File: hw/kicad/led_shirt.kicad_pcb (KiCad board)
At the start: 2 copper layers, 26 parts, among them J1 10103593-0001LF, J2 2_PIN_HDR, J3 2_PIN_HDR, J4 5_PIN_HDR, Q1 PN_MOSFET_DUAL, SW1 SW_PUSH, U1 AP3012, U2 PIC12F1822, U3 MCP73831

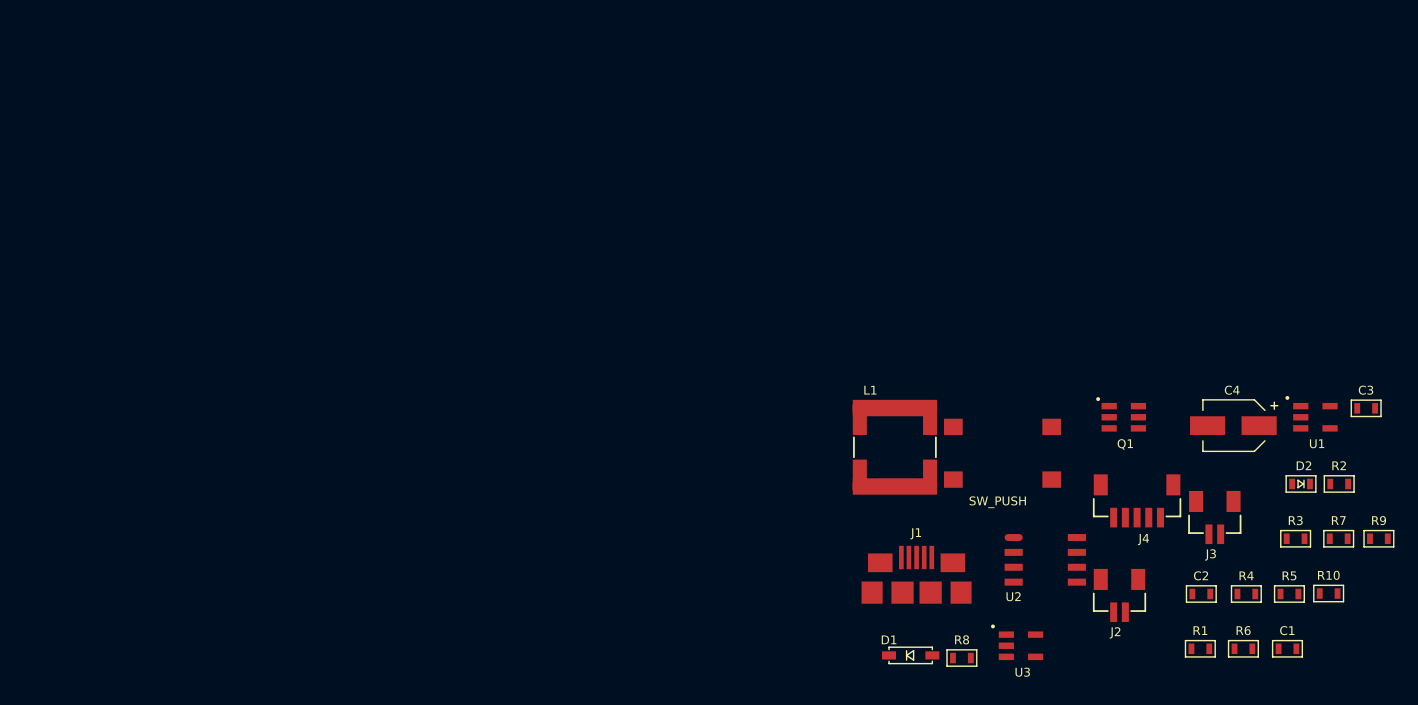
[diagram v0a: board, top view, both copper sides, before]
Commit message: parts positioned, silks. next is traces.
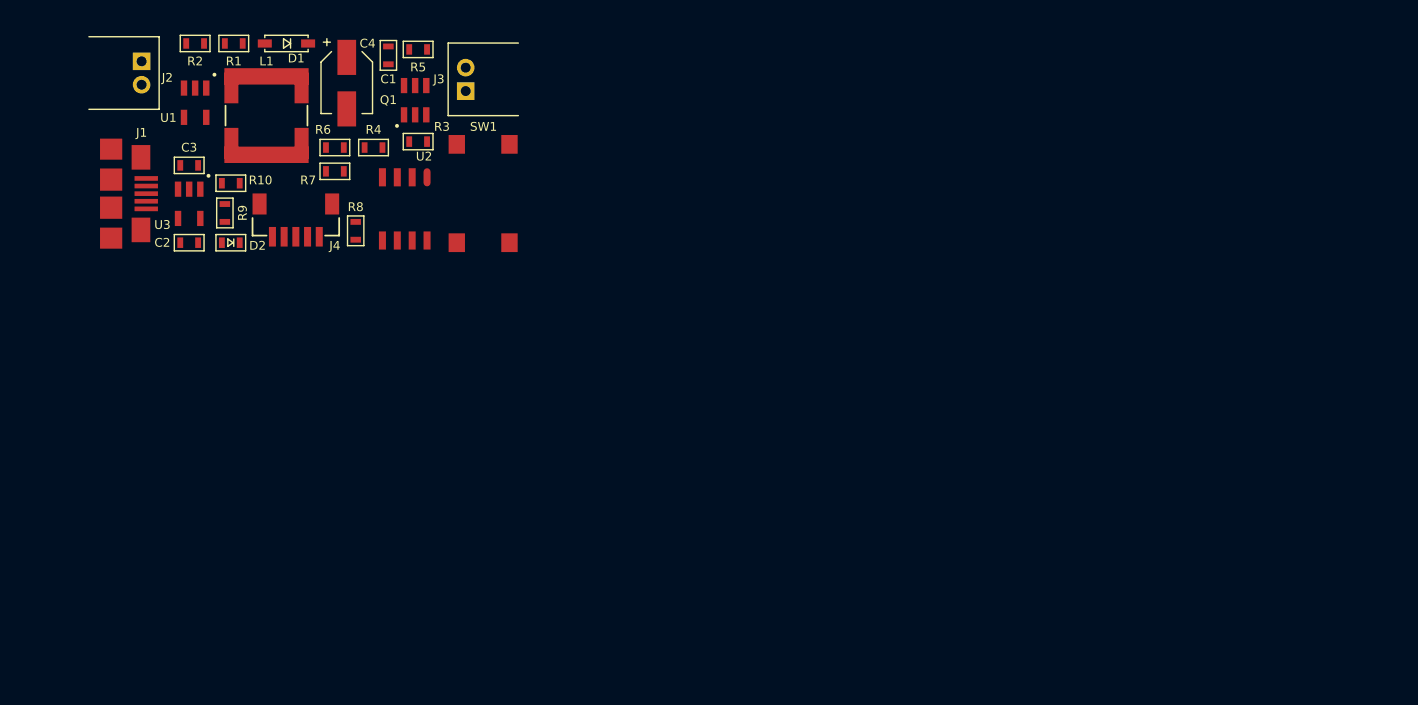
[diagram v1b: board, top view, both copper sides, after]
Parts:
- J2, J3: footprint kicadlib:SMD_JST_2_PIN_VERT -> kicadlib:TH_JST_2PIN_RIGHTANGLE
- moved R2 106.1 mm to (125.0, 79.0), turned to 180 degrees
- moved R9 103.4 mm to (128.3, 92.7), turned to 90 degrees
- moved C3 102.7 mm to (126.0, 89.4)
- moved R10 101.5 mm to (128.0, 90.9), turned to 180 degrees
- moved R1 98.7 mm to (128.3, 79.0), turned to 180 degrees
- moved U1 98.5 mm to (125.7, 82.8), turned to 270 degrees
- moved J2 95.4 mm to (121.2, 80.5), turned to 270 degrees
- moved D2 93.7 mm to (129.5, 96.0)
- moved C2 93.0 mm to (124.5, 96.0), turned to 180 degrees
- moved R7 92.7 mm to (136.9, 89.9), turned to 180 degrees
- moved C1 92.2 mm to (142.2, 80.8), turned to 270 degrees
- moved R6 90.0 mm to (136.9, 87.9), turned to 180 degrees
- moved R5 89.1 mm to (144.0, 79.5), turned to 180 degrees
- moved R4 85.1 mm to (140.2, 87.9), turned to 180 degrees
- moved R3 83.7 mm to (144.0, 87.4), turned to 180 degrees
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
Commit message: layout done
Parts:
- moved R5 1.48 mm to (144.8, 80.8), turned to 270 degrees
- moved U1 0.51 mm to (125.2, 82.8)
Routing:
- net GND: track 0.00 -> 76.3 mm, vias 0 -> 11
- net /vbat: track 0.00 -> 67.3 mm, vias 0 -> 1
- net /lps: track 0.00 -> 38.1 mm, vias 0 -> 3
- net /~lps_enable: track 0.00 -> 25.8 mm
- net /+12v: track 0.00 -> 22.5 mm
- net /icspdat: track 0.00 -> 15.9 mm, vias 0 -> 2
- net /led_cntrl: track 0.00 -> 14.1 mm, vias 0 -> 2
- net Net-(D1-Pad2): track 0.00 -> 13.8 mm
- net /icspclk: track 0.00 -> 12.7 mm, vias 0 -> 2
- net /mclr: track 0.00 -> 11.9 mm
- net /vbus: track 0.00 -> 10.8 mm
- net /batt_sns: track 0.00 -> 6.62 mm
- net Net-(R1-Pad2): track 0.00 -> 6.51 mm
- net Net-(D2-Pad2): track 0.00 -> 5.08 mm
- net /led-: track 0.00 -> 4.81 mm
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- added copper zone on B.Cu, net GND
- added copper zone on F.Cu, net GND

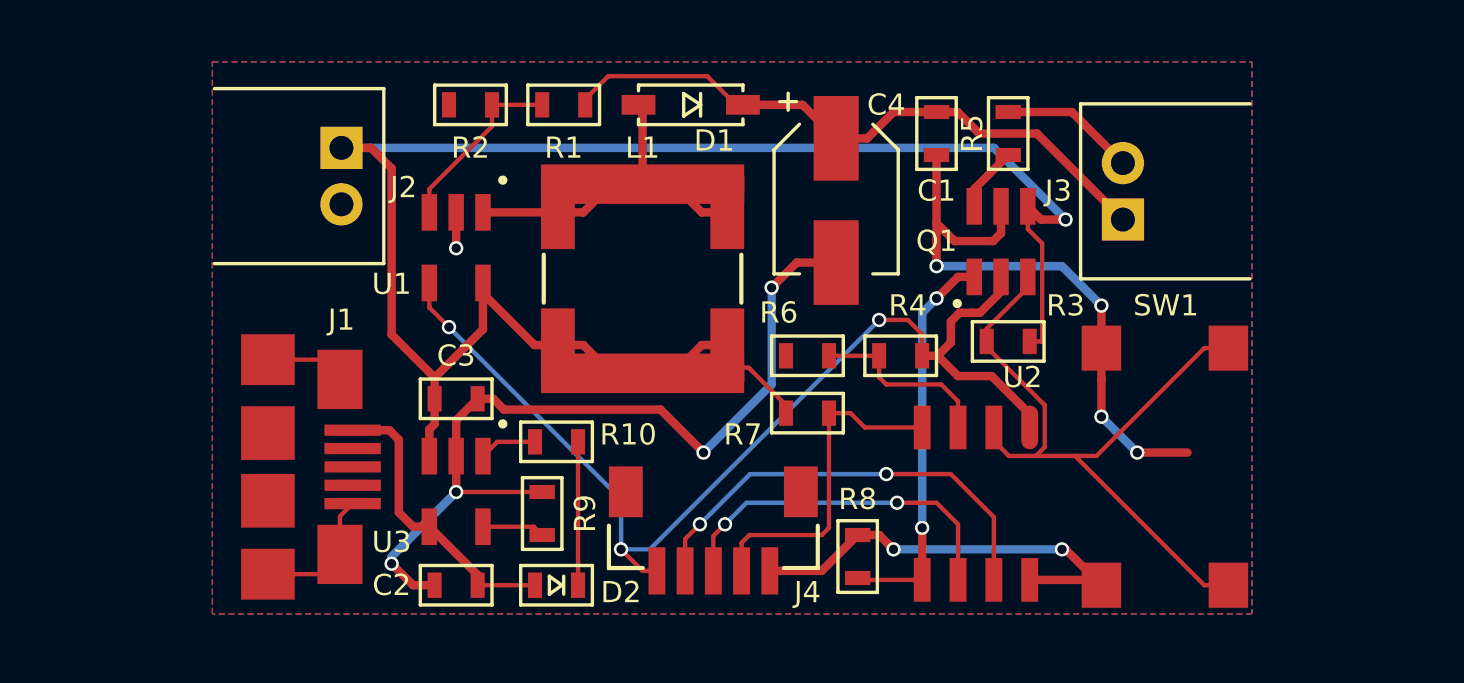
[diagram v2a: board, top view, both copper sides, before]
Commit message: add screw mounts, which adds $1.60 to osh price. also need to reposition usb connector if I use screw mounts.
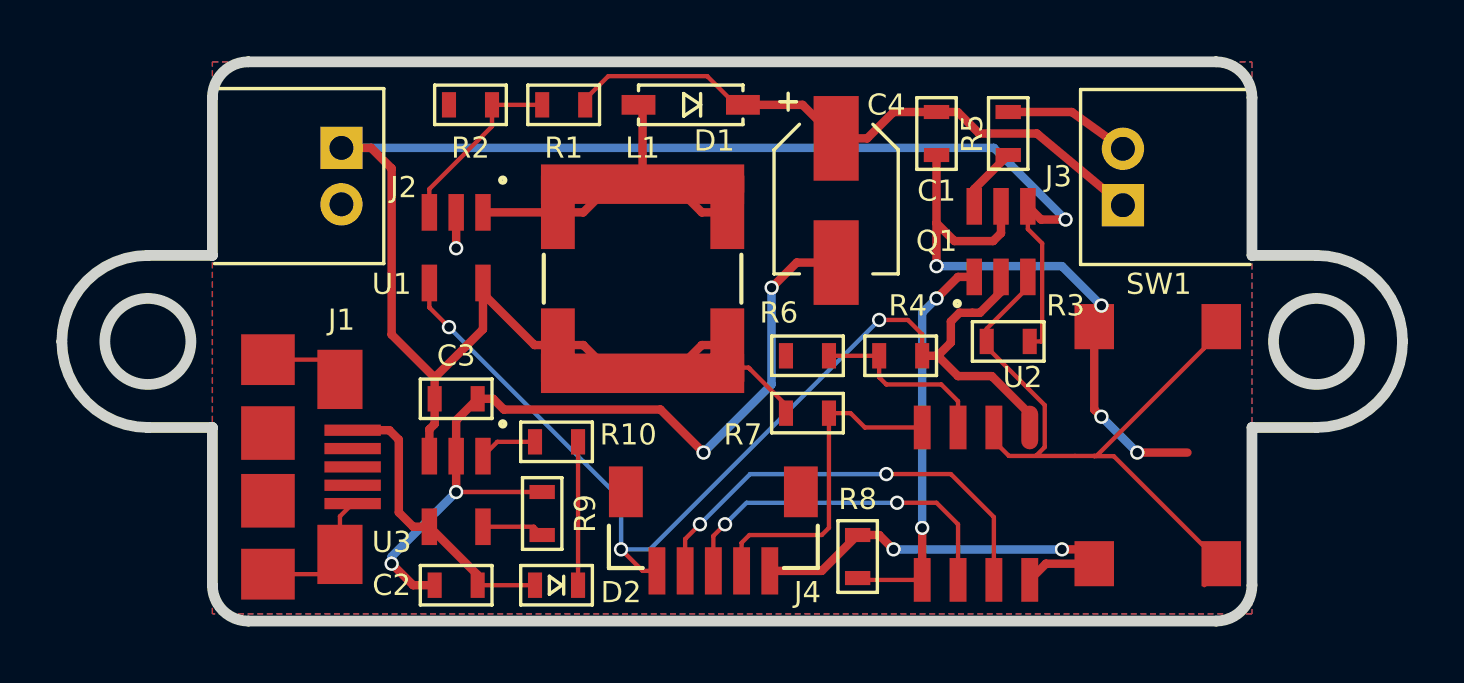
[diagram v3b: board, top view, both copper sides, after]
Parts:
- moved SW1 0.80 mm to (147.8, 95.2)
- moved J3 0.51 mm to (148.8, 82.5)
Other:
- board outline added: 47.5 x 19.8 mm
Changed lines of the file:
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@@
-(kicad_pcb (version 4) (host pcbnew 4.0.0-rc1-stable)
+(kicad_pcb (version 4) (host pcbnew 4.0.0-rc2-stable)
   (general
     (links 67)
     (no_connects 0)
-    (area 115.34578 76.46528 153.703721 98.16672)
+    (area 111.061499 77.279499 158.940501 97.472501)
     (thickness 1.6002)
-    (drawings 0)
-    (tracks 226)
+    (drawings 20)
+    (tracks 231)
     (zones 0)
     (modules 26)
@@
   )
   (module kicadlib:TH_JST_2PIN_RIGHTANGLE (layer Front)
-    (at 148.844 83.058 90)
+    (at 148.844 82.55 90)
     (fp_text reference J3 (at 1.016 -2.286 180) (layer F.SilkS)
       (effects (font (size 0.75 0.75) (thickness 0.12)))
@@
   )
   (module kicadlib:spst_pushbutton_smd placed (layer Front)
-    (at 148.082 96.012 90)
+    (at 147.828 95.25 90)
     (fp_text reference SW1 (at 9.906 2.286 180) (layer F.SilkS)
       (effects (font (size 0.75 0.75) (thickness 0.12)))
@@
     )
   )
-  (segment (start 145.796 80.01) (end 148.844 83.058) (width 0.29972) (layer Front) (net 1))
+  (gr_line (start 116.586 90.424) (end 116.586 96.012) (angle 90) (layer Edge.Cuts) (width 0.381))
+  (gr_line (start 116.586 78.74) (end 116.586 84.328) (angle 90) (layer Edge.Cuts) (width 0.381))
+  (gr_line (start 153.416 90.424) (end 153.416 96.012) (angle 90) (layer Edge.Cuts) (width 0.381))
+  (gr_line (start 153.416 78.74) (end 153.416 84.328) (angle 90) (layer Edge.Cuts) (width 0.381))
+  (gr_circle (center 114.3 87.376) (end 114.3 85.852) (layer Edge.Cuts) (width 0.381))
+  (gr_arc (start 114.3 87.376) (end 114.3 90.424) (angle 90) (layer Edge.Cuts) (width 0.381))
+  (gr_arc (start 114.3 87.376) (end 111.252 87.376) (angle 90) (layer Edge.Cuts) (width 0.381))
+  (gr_line (start 114.3 90.424) (end 116.586 90.424) (angle 90) (layer Edge.Cuts) (width 0.381))
+  (gr_line (start 114.3 84.328) (end 116.586 84.328) (angle 90) (layer Edge.Cuts) (width 0.381))
+  (gr_line (start 117.856 97.282) (end 152.146 97.282) (angle 90) (layer Edge.Cuts) (width 0.381))
+  (gr_line (start 155.702 90.424) (end 153.416 90.424) (angle 90) (layer Edge.Cuts) (width 0.381))
+  (gr_line (start 155.702 84.328) (end 153.416 84.328) (angle 90) (layer Edge.Cuts) (width 0.381))
+  (gr_arc (start 155.702 87.376) (end 158.75 87.376) (angle 90) (layer Edge.Cuts) (width 0.381))
+  (gr_arc (start 155.702 87.376) (end 155.702 84.328) (angle 90) (layer Edge.Cuts) (width 0.381))
+  (gr_circle (center 155.702 87.376) (end 155.702 88.9) (layer Edge.Cuts) (width 0.381))
+  (gr_line (start 152.146 77.47) (end 117.856 77.47) (angle 90) (layer Edge.Cuts) (width 0.381))
+  (gr_arc (start 117.856 96.012) (end 117.856 97.282) (angle 90) (layer Edge.Cuts) (width 0.381))
+  (gr_arc (start 152.146 96.012) (end 153.416 96.012) (angle 90) (layer Edge.Cuts) (width 0.381))
+  (gr_arc (start 152.146 78.74) (end 152.146 77.47) (angle 90) (layer Edge.Cuts) (width 0.381))
+  (gr_arc (start 117.856 78.74) (end 116.586 78.74) (angle 90) (layer Edge.Cuts) (width 0.381))
+  (segment (start 145.796 80.01) (end 148.844 82.55) (width 0.29972) (layer Front) (net 1) (status 20))
   (segment (start 143.75172 80.01) (end 145.796 80.01) (width 0.29972) (layer Front) (net 1))
   (segment (start 142.24 79.248) (end 142.98972 79.248) (width 0.29972) (layer Front) (net 1))
@@
   (segment (start 134.116 77.978) (end 135.132 78.994) (width 0.15494) (layer Front) (net 1))
   (segment (start 135.132 78.994) (end 135.382 78.994) (width 0.15494) (layer Front) (net 1))
+  (segment (start 148.082 90.043) (end 147.828 89.789) (width 0.29972) (layer Front) (net 2))
+  (via (at 148.082 90.043) (size 0.508) (drill 0.3302) (layers Front Back) (net 2))
+  (via (at 149.352 91.313) (size 0.508) (drill 0.3302) (layers Front Back) (net 2))
+  (segment (start 148.082 90.043) (end 149.352 91.313) (width 0.29972) (layer Back) (net 2))
+  (segment (start 151.13 91.313) (end 149.352 91.313) (width 0.29972) (layer Front) (net 2))
+  (segment (start 147.828 89.789) (end 147.828 86.85) (width 0.29972) (layer Front) (net 2))
+  (segment (start 145.542 95.824) (end 146.116 95.25) (width 0.29972) (layer Front) (net 2))
+  (segment (start 146.116 95.25) (end 147.828 95.25) (width 0.29972) (layer Front) (net 2))
+  (segment (start 146.685 94.742) (end 147.32 94.742) (width 0.29972) (layer Front) (net 2))
+  (segment (start 147.32 94.742) (end 147.828 95.25) (width 0.29972) (layer Front) (net 2))
+  (segment (start 146.685 94.742) (end 146.812 94.742) (width 0.29972) (layer Front) (net 2))
+  (segment (start 140.208 94.234) (end 140.716 94.742) (width 0.29972) (layer Front) (net 2))
+  (via (at 140.716 94.742) (size 0.508) (drill 0.3302) (layers Front Back) (net 2))
+  (segment (start 140.716 94.742) (end 146.685 94.742) (width 0.29972) (layer Back) (net 2))
+  (via (at 146.685 94.742) (size 0.508) (drill 0.3302) (layers Front Back) (net 2))
+  (segment (start 139.446 94.234) (end 140.208 94.234) (width 0.29972) (layer Front) (net 2))
   (segment (start 128.27 92.71) (end 125.222 92.71) (width 0.15494) (layer Front) (net 2))
-  (segment (start 146.685 94.742) (end 146.812 94.742) (width 0.29972) (layer Front) (net 2))
-  (segment (start 139.446 94.234) (end 140.208 94.234) (width 0.29972) (layer Front) (net 2))
-  (via (at 146.685 94.742) (size 0.508) (drill 0.3302) (layers Front Back) (net 2))
-  (segment (start 140.716 94.742) (end 146.685 94.742) (width 0.29972) (layer Back) (net 2))
-  (via (at 140.716 94.742) (size 0.508) (drill 0.3302) (layers Front Back) (net 2))
-  (segment (start 140.208 94.234) (end 140.716 94.742) (width 0.29972) (layer Front) (net 2))
-  (segment (start 146.812 94.742) (end 148.082 96.012) (width 0.29972) (layer Front) (net 2))
-  (segment (start 145.542 95.824) (end 147.894 95.824) (width 0.29972) (layer Front) (net 2))
-  (segment (start 147.894 95.824) (end 148.082 96.012) (width 0.29972) (layer Front) (net 2))
+  (segment (start 147.64 95.062) (end 147.828 95.25) (width 0.29972) (layer Front) (net 2) (status 30))
   (segment (start 136.334 95.504) (end 138.176 95.504) (width 0.29972) (layer Front) (net 2))
   (segment (start 138.176 95.504) (end 139.446 94.234) (width 0.29972) (layer Front) (net 2))
@@
   (segment (start 137.287 84.582) (end 136.398 85.471) (width 0.29972) (layer Front) (net 2))
   (via (at 136.398 85.471) (size 0.508) (drill 0.3302) (layers Front Back) (net 2))
-  (segment (start 148.082 86.106) (end 148.082 87.612) (width 0.29972) (layer Front) (net 2))
+  (segment (start 148.082 86.106) (end 147.828 86.85) (width 0.29972) (layer Front) (net 2) (status 20))
   (segment (start 142.24 84.709) (end 146.685 84.709) (width 0.29972) (layer Back) (net 2))
   (segment (start 146.685 84.709) (end 148.082 86.106) (width 0.29972) (layer Back) (net 2))
@@
   (segment (start 142.24 83.185) (end 142.875 83.82) (width 0.29972) (layer Front) (net 2))
   (segment (start 142.24 80.772) (end 142.24 83.185) (width 0.29972) (layer Front) (net 2))
-  (segment (start 149.352 91.313) (end 151.13 91.313) (width 0.29972) (layer Front) (net 2))
-  (segment (start 148.082 90.043) (end 149.352 91.313) (width 0.29972) (layer Back) (net 2))
-  (via (at 149.352 91.313) (size 0.508) (drill 0.3302) (layers Front Back) (net 2))
-  (segment (start 148.082 88.71172) (end 148.082 90.043) (width 0.29972) (layer Front) (net 2))
-  (via (at 148.082 90.043) (size 0.508) (drill 0.3302) (layers Front Back) (net 2))
-  (segment (start 148.082 87.612) (end 148.082 88.71172) (width 0.29972) (layer Front) (net 2))
   (segment (start 132.461 89.789) (end 133.985 91.313) (width 0.29972) (layer Front) (net 2))
   (segment (start 126.91472 89.789) (end 132.461 89.789) (width 0.29972) (layer Front) (net 2))
@@
   (segment (start 141.732 95.824) (end 139.512 95.824) (width 0.15494) (layer Front) (net 13))
   (segment (start 139.512 95.824) (end 139.446 95.758) (width 0.15494) (layer Front) (net 13))
-  (segment (start 152.582 87.612) (end 151.72706 87.612) (width 0.15494) (layer Front) (net 14))
+  (segment (start 152.328 95.25) (end 148.518 91.44) (width 0.15494) (layer Front) (net 14))
+  (segment (start 147.828 91.44) (end 147.828 91.43142) (width 0.15494) (layer Front) (net 14))
+  (segment (start 148.518 91.44) (end 147.828 91.44) (width 0.15494) (layer Front) (net 14))
+  (segment (start 152.328 86.85) (end 151.72706 87.612) (width 0.15494) (layer Front) (net 14) (status 10))
   (segment (start 151.72706 87.612) (end 147.90764 91.43142) (width 0.15494) (layer Front) (net 14))
-  (segment (start 147.90764 91.43142) (end 147.14648 91.43142) (width 0.15494) (layer Front) (net 14))
-  (segment (start 152.582 96.012) (end 151.72706 96.012) (width 0.15494) (layer Front) (net 14))
-  (segment (start 151.72706 96.012) (end 147.14648 91.43142) (width 0.15494) (layer Front) (net 14))
+  (segment (start 147.90764 91.43142) (end 147.828 91.43142) (width 0.15494) (layer Front) (net 14))
+  (segment (start 147.828 91.43142) (end 147.14648 91.43142) (width 0.15494) (layer Front) (net 14))
   (segment (start 147.14648 91.43142) (end 145.762535 91.43142) (width 0.15494) (layer Front) (net 14))
+  (segment (start 152.328 95.25) (end 151.72706 96.012) (width 0.15494) (layer Front) (net 14) (status 10))
   (segment (start 144.018 87.376) (end 144.018 87.576) (width 0.15494) (layer Front) (net 14))
   (segment (start 144.018 87.576) (end 146.07442 89.63242) (width 0.15494) (layer Front) (net 14))
@@
   (segment (start 140.208 87.884) (end 138.43 87.884) (width 0.15494) (layer Front) (net 17))
   (segment (start 144.78 79.248) (end 147.034 79.248) (width 0.29972) (layer Front) (net 18))
-  (segment (start 147.034 79.248) (end 148.844 81.058) (width 0.29972) (layer Front) (net 18))
+  (segment (start 147.034 79.248) (end 148.844 80.55) (width 0.29972) (layer Front) (net 18) (status 20))
   (segment (start 126.172 93.94) (end 127.976 93.94) (width 0.15494) (layer Front) (net 19))
   (segment (start 127.976 93.94) (end 128.27 94.234) (width 0.15494) (layer Front) (net 19))
